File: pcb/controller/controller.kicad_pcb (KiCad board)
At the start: 2 copper layers, 100 x 100 mm, 62 parts, among them J1 Conn_01x06, J2 Pogo_01x06_male, J3 G-Switch GT-USB-7010ASV, J5 0.91 OLED, Q1 BSS138, Q2 BSS138, SW1 B3F-4055, SW2 B3F-4055, SW3 B3F-4055, U1 XIAO-ESP32-C6-SMD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

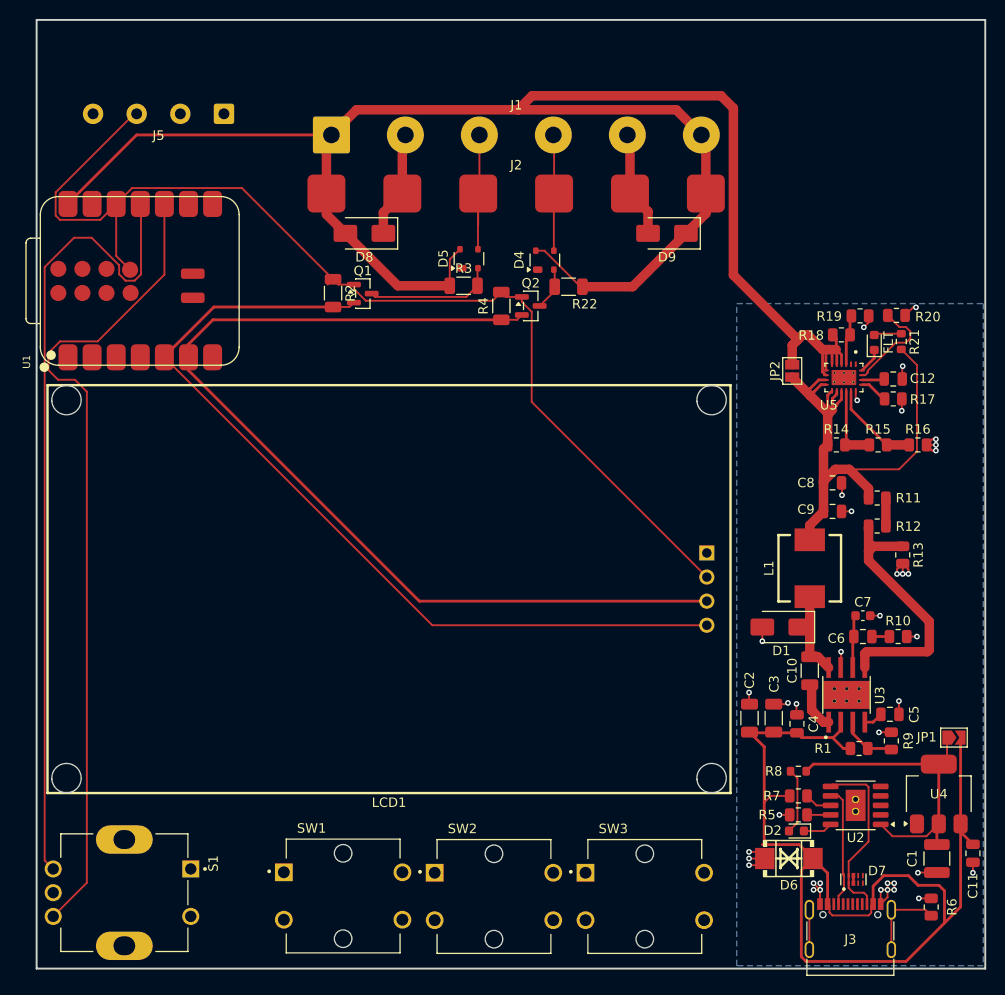
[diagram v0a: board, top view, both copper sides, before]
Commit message: traced controller pcb and renamed to Blitzpong
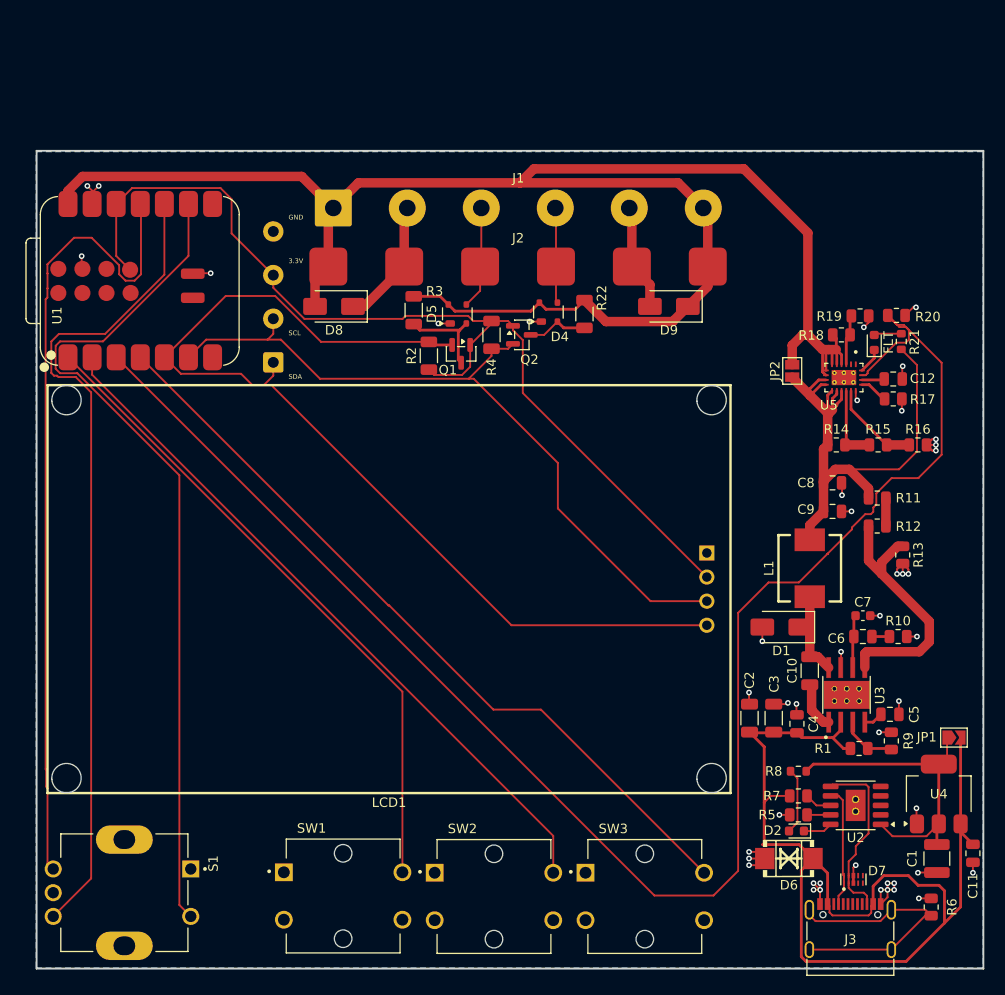
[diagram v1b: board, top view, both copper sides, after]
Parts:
- J5: moved to B.Cu
- moved J5 26.7 mm to (207.8, 99.2), turned to 90 degrees
- moved Q1 12.2 mm to (227.6, 98.3), turned to -90 degrees
- moved R2 12.1 mm to (224.2, 98.5), turned to 90 degrees
- moved D8 8.34 mm to (214.2, 93.3)
- moved D9 7.70 mm to (249.5, 93.3)
- moved J1 7.70 mm to (214.1, 82.9)
- moved J2 7.70 mm to (233.6, 89.1)
- moved D5 5.95 mm to (227.2, 94.1)
- moved R3 5.86 mm to (222.6, 93.7), turned to -90 degrees
- moved D4 5.49 mm to (236.8, 93.9)
- moved R22 3.33 mm to (240.6, 94.1), turned to -90 degrees
- moved R4 3.22 mm to (230.8, 96.3)
- moved Q2 3.19 mm to (234.0, 96.3)
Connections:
- U1 pad 1: Imon -> /Inputs/SW1
- U1 pad 2: /Inputs/SW1 -> /Inputs/SW2
- U1 pad 3: /Inputs/SW2 -> Imon
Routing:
- net Imon: track 10.6 -> 174.7 mm
- net /Inputs/SW4: track 0.00 -> 90.5 mm
- net /Inputs/SW3: track 0.00 -> 81.9 mm
- net /Inputs/SW2: track 0.00 -> 74.5 mm
- net /Inputs/SW1: track 0.00 -> 68.9 mm
- net SCL: track 103.9 -> 78.7 mm
- net SDA: track 91.3 -> 106.8 mm
- net Net-(J3-SHIELD): track 13.6 -> 28.8 mm
- net GND: track 74.8 -> 89.9 mm, vias 38 -> 46
- net +3.3V: track 116.8 -> 104.9 mm
- net +5V: track 203.0 -> 191.8 mm
- net Net-(D5-I/O2): track 15.4 -> 10.8 mm
- net /Target Interface/Level Shifter/HC: track 13.7 -> 9.73 mm
- net Net-(D4-I/O2): track 12.2 -> 10.1 mm
- net /Target Interface/Level Shifter1/HC: track 4.52 -> 6.52 mm
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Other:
- board size 100 x 100 mm -> 99.8 x 86.2 mm
- board text added: "3.3V"
- board text added: "GND"
- board text added: "SCL"
- board text added: "SDA"

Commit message: finished all pcbs by adjusting traces acording to 1oz copper weight
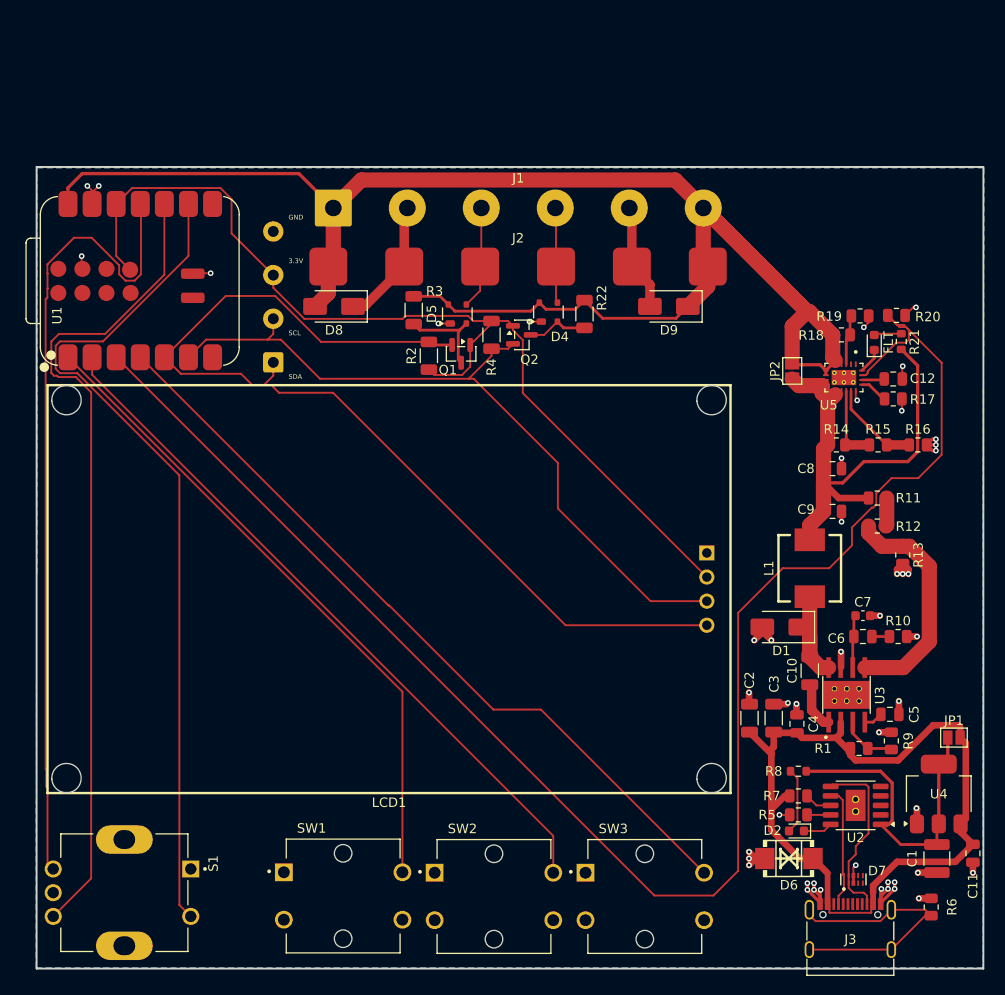
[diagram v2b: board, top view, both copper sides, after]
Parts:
- JP1: footprint Jumper:SolderJumper-2_P1.3mm_Open_TrianglePad1.0x1.5mm -> Jumper:SolderJumper-2_P1.3mm_Open_Pad1.0x1.5mm
- moved C8 1.50 mm to (266.8, 110.4)
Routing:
- net /Power Input/Buck/VIN: track 111.7 -> 86.0 mm
- net +5V: track 191.8 -> 177.3 mm
- net /Power Input/Buck/VOUT: track 58.8 -> 53.1 mm
- net Net-(U3-VSENSE): track 27.8 -> 24.5 mm
- net GND: track 89.9 -> 92.6 mm, vias 46 -> 48
- net Net-(D1-K): track 8.80 -> 10.9 mm
- net Net-(JP1-A): track 33.2 -> 35.0 mm
- net Imon: track 174.7 -> 175.4 mm
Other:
- board size 99.8 x 86.2 mm -> 99.8 x 84.5 mm

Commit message: exported all pcbs
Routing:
- net Net-(D1-K): track 10.9 -> 14.6 mm
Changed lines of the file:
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@@
 			(plot_on_all_layers_selection 0x00000000_00000000_00000000_00000000)
 			(disableapertmacros no)
-			(usegerberextensions no)
+			(usegerberextensions yes)
 			(usegerberattributes yes)
 			(usegerberadvancedattributes yes)
@@
 			(sketchdnponfab yes)
 			(crossoutdnponfab yes)
-			(subtractmaskfromsilk no)
+			(subtractmaskfromsilk yes)
 			(outputformat 1)
 			(mirror no)
-			(drillshape 1)
+			(drillshape 0)
 			(scaleselection 1)
-			(outputdirectory "")
+			(outputdirectory "export/")
 		)
 	)
@@
 	)
 	(gr_text "3.3V"
-		(at 209.4 88.8 0)
+		(at 209.1 91.9 0)
 		(layer "F.SilkS")
 		(effects
 			(font
-				(size 0.5 0.5)
-				(thickness 0.0625)
+				(size 0.8 0.8)
+				(thickness 0.1)
 			)
 			(justify left bottom)
@@
 	)
 	(gr_text "SCL"
-		(at 209.4 96.4 0)
+		(at 209.4 96.8 0)
 		(layer "F.SilkS")
 		(effects
 			(font
-				(size 0.5 0.5)
-				(thickness 0.0625)
+				(size 0.8 0.8)
+				(thickness 0.1)
 			)
 			(justify left bottom)
@@
 	)
 	(gr_text "GND"
-		(at 209.4 84.2 0)
+		(at 209.3 86.8 0)
 		(layer "F.SilkS")
 		(effects
 			(font
-				(size 0.5 0.5)
-				(thickness 0.0625)
+				(size 0.8 0.8)
+				(thickness 0.1)
 			)
 			(justify left bottom)
@@
 		(effects
 			(font
-				(size 0.5 0.5)
-				(thickness 0.0625)
+				(size 0.8 0.8)
+				(thickness 0.1)
 			)
 			(justify left bottom)
@@
 	)
 	(segment
-		(start 265.43 154.87)
-		(end 265.5 154.8)
-		(width 0.35)
-		(layer "F.Cu")
-		(net 2)
-	)
-	(segment
 		(start 245.6 83.2)
 		(end 245.325 82.925)
@@
 	)
 	(segment
+		(start 265.4 154.84)
+		(end 265.43 154.87)
+		(width 0.35)
+		(layer "F.Cu")
+		(net 2)
+	)
+	(segment
 		(start 276.6625 107.9)
 		(end 277.65 107.9)
@@
 	)
 	(segment
+		(start 265.4 154.5)
+		(end 265.4 154.84)
+		(width 0.35)
+		(layer "F.Cu")
+		(net 2)
+	)
+	(segment
 		(start 261.925 135.225)
 		(end 262.05 135.1)
@@
 	)
 	(segment
+		(start 265.43 154.87)
+		(end 265.43 156.3)
+		(width 0.35)
+		(layer "F.Cu")
+		(net 2)
+	)
+	(segment
 		(start 275.65 147.85)
 		(end 275.65 146.25)
@@
 	)
 	(segment
-		(start 265.43 156.3)
-		(end 265.43 154.87)
-		(width 0.35)
-		(layer "F.Cu")
-		(net 2)
-	)
-	(segment
 		(start 274.0625 103.05)
 		(end 274.0625 104.2875)
@@
 	)
 	(via
-		(at 265.5 154.8)
+		(at 265.4 154.5)
 		(size 0.6)
 		(drill 0.3)
@@
 	)
 	(segment
+		(start 265.5 131.375)
+		(end 264.35 130.225)
+		(width 0.7)
+		(layer "F.Cu")
+		(net 8)
+	)
+	(segment
+		(start 266.345 131.375)
+		(end 266.345 129.745)
+		(width 0.7)
+		(layer "F.Cu")
+		(net 8)
+	)
+	(segment
+		(start 266.345 129.745)
+		(end 266.2 129.6)
+		(width 0.7)
+		(layer "F.Cu")
+		(net 8)
+	)
+	(segment
 		(start 266.345 131.375)
 		(end 265.5 131.375)
-		(width 1.6)
+		(width 0.7)
 		(layer "F.Cu")
 		(net 8)
 	)
 	(segment
-		(start 264.35 130.225)
+		(start 264.35 129.6)
 		(end 264.35 128.1)
 		(width 1.6)
@@
 	)
 	(segment
-		(start 265.5 131.375)
-		(end 264.35 130.225)
+		(start 264.35 130.225)
+		(end 264.35 129.6)
 		(width 1.6)
 		(layer "F.Cu")
@@
 	)
 	(segment
+		(start 266.2 129.6)
+		(end 264.35 129.6)
+		(width 0.7)
+		(layer "F.Cu")
+		(net 8)
+	)
+	(segment
 		(start 264.55 135.877)
 		(end 265.798 137.125)
@@
 	)
 	(segment
-		(start 276.951 120.6885)
-		(end 274.85 118.5875)
-		(width 1.6)
+		(start 271.9875 118.5875)
+		(end 274.15 118.5875)
+		(width 0.7)
 		(layer "F.Cu")
 		(net 32)
 	)
 	(segment
-		(start 274.85 118.5875)
-		(end 274.15 118.5875)
-		(width 1.6)
+		(start 270.55 117.15)
+		(end 271.9875 118.5875)
+		(width 0.7)
 		(layer "F.Cu")
 		(net 32)
 	)
 	(segment
-		(start 270.155 131.375)
-		(end 274.214892 131.375)
-		(width 1.6)
+		(start 274.15 118.5875)
+		(end 274.85 118.5875)
+		(width 0.7)
 		(layer "F.Cu")
 		(net 32)
 	)
 	(segment
-		(start 270.55 116.45)
-		(end 270.55 117.171998)
-		(width 1.6)
+		(start 276.551 120.2885)
+		(end 276.551 129.109603)
+		(width 0.7)
 		(layer "F.Cu")
 		(net 32)
 	)
 	(segment
-		(start 271.965502 118.5875)
-		(end 274.15 118.5875)
-		(width 1.6)
+		(start 274.85 118.5875)
+		(end 276.551 120.2885)
+		(width 0.7)
 		(layer "F.Cu")
 		(net 32)
 	)
 	(segment
-		(start 274.214892 131.375)
-		(end 276.951 128.638892)
-		(width 1.6)
+		(start 270.155 131.375)
+		(end 274.285603 131.375)
+		(width 0.7)
 		(layer "F.Cu")
 		(net 32)
 	)
 	(segment
-		(start 270.55 117.171998)
-		(end 271.965502 118.5875)
-		(width 1.6)
+		(start 276.551 129.109603)
+		(end 274.285603 131.375)
+		(width 0.7)
 		(layer "F.Cu")
 		(net 32)
 	)
 	(segment
-		(start 276.951 128.638892)
-		(end 276.951 120.6885)
-		(width 1.6)
+		(start 270.55 116.45)
+		(end 270.55 117.15)
+		(width 0.7)
 		(layer "F.Cu")
 		(net 32)
